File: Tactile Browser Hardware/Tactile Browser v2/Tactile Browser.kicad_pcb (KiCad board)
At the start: 2 copper layers, 100.5 x 125 mm, 79 parts, among them SW1 SW_Push, SW10 SW_Push, SW11 SW_Push, SW12 SW_Push, SW13 SW_Push, SW14 SW_Push, SW15 SW_Push, SW16 SW_Push, SW17 SW_Push, SW18 SW_Push, SW19 SW_Push, SW2 SW_Push, SW20 SW_Push, SW3 SW_Push, SW4 SW_Push, SW5 SW_Push, SW6 SW_Push, SW7 SW_Push, SW8 SW_Push, SW9 SW_Push

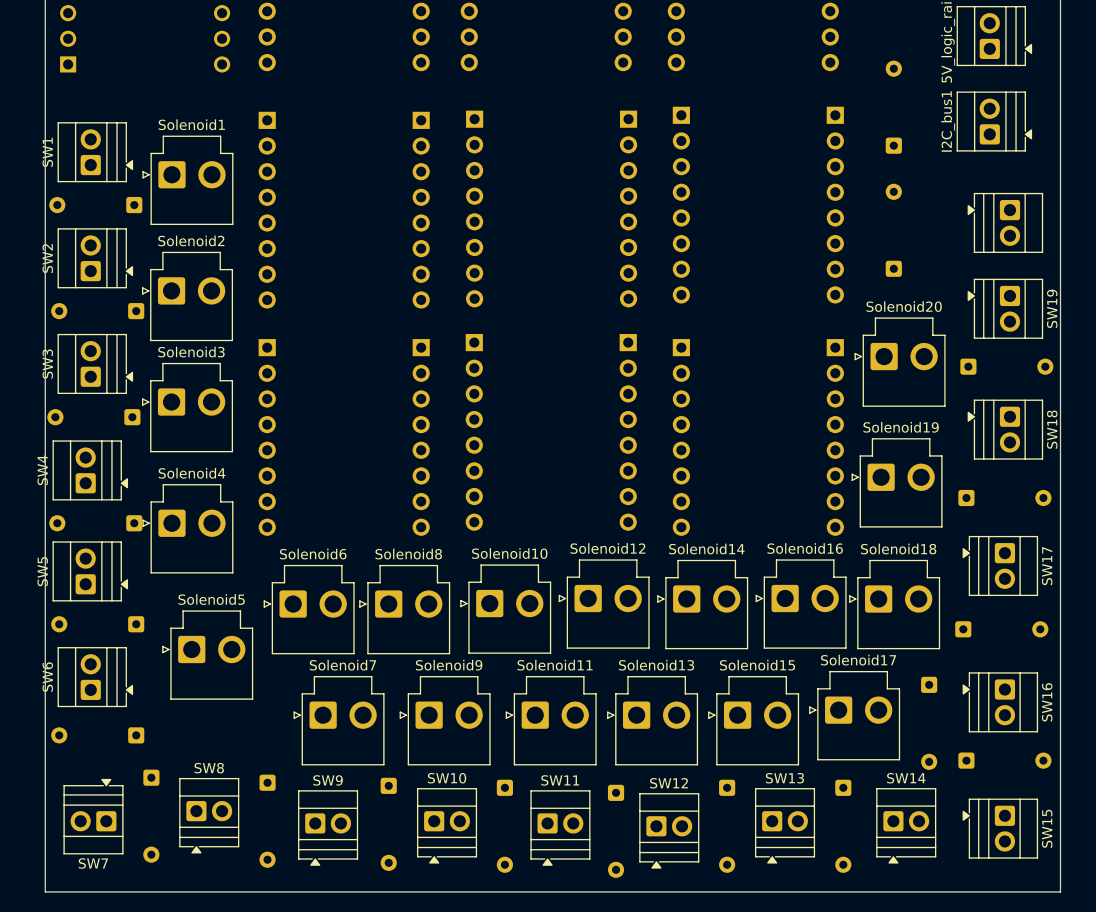
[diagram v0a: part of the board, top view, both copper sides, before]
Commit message: updated solenoid/keyswitch connectors
for ease of manufacturing
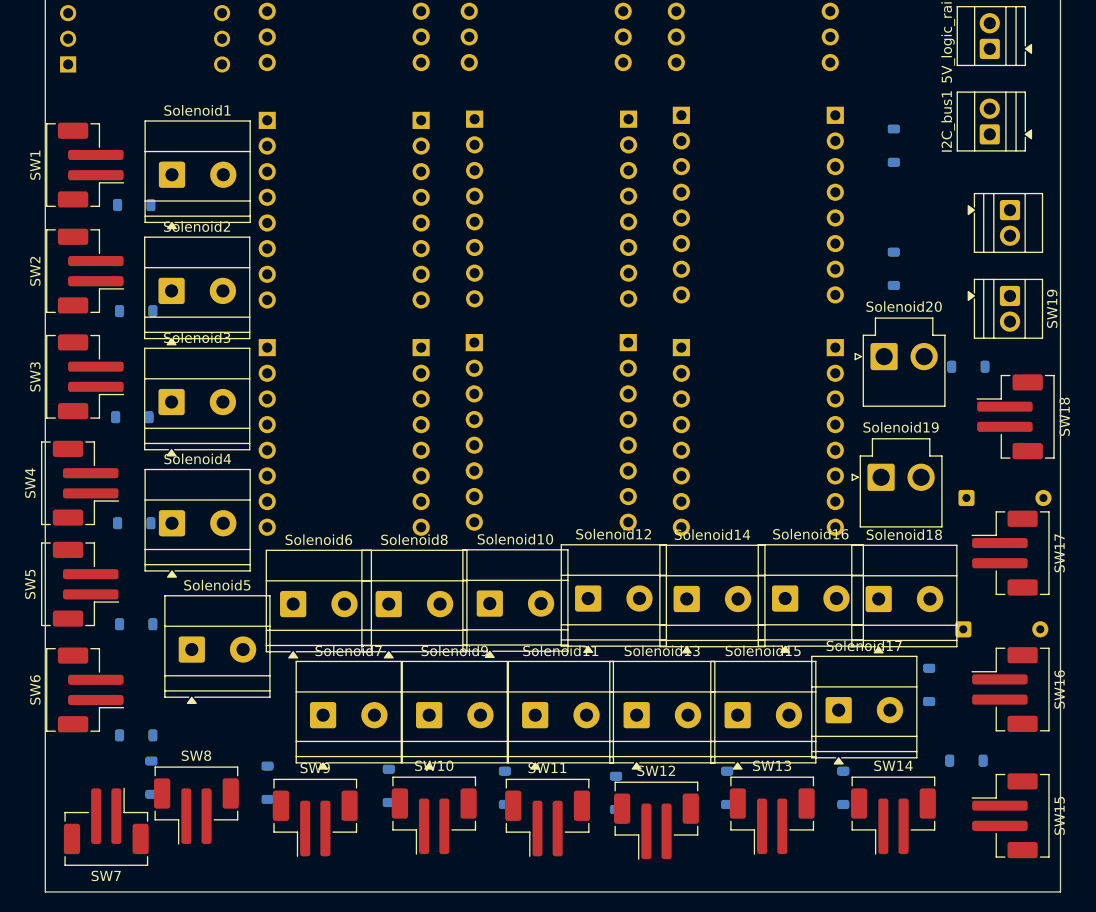
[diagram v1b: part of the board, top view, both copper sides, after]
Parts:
- D1, D10, D11, D12, D13, D14, D15, D18, D19, D2, D20, D3, D4, D5, D6, D7, D8, D9: footprint Diode_THT:D_DO-35_SOD27_P7.62mm_Horizontal -> Diode_SMD:D_SOD-123
- SW1, SW10, SW11, SW12, SW13, SW14, SW15, SW16, SW17, SW18, SW2, SW3, SW4, SW5, SW6, SW7, SW8, SW9: footprint TerminalBlock:TerminalBlock_Xinya_XY308-2.54-2P_1x02_P2.54mm_Horizontal -> Connector_JST:JST_PH_B2B-PH-SM4-TB_1x02-1MP_P2.00mm_Vertical
- Solenoid1: footprint Connector_JST:JST_VH_B2P-VH_1x02_P3.96mm_Vertical -> TerminalBlock_Phoenix:TerminalBlock_Phoenix_MKDS-1,5-2-5.08_1x02_P5.08mm_Horizontal
- Solenoid10, Solenoid11, Solenoid12, Solenoid13, Solenoid14, Solenoid15, Solenoid16, Solenoid17, Solenoid18, Solenoid2, Solenoid3, Solenoid4, Solenoid5, Solenoid6, Solenoid7, Solenoid8, Solenoid9: footprint Connector_JST:JST_VH_B2P-VH-B_1x02_P3.96mm_Vertical -> TerminalBlock_Phoenix:TerminalBlock_Phoenix_MKDS-1,5-2-5.08_1x02_P5.08mm_Horizontal
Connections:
- A1 pad 1: Row2 -> Col2
- A1 pad 10: Col4 -> Row5
- A1 pad 11: Col5 -> Row6
- A1 pad 2: Row1 -> Col1
- A1 pad 5: Row3 -> Col3
- A1 pad 6: Row4 -> Row1
- A1 pad 7: Col1 -> Row2
- A1 pad 8: Col2 -> Row3
- A1 pad 9: Col3 -> Row4
- D1 pad 1: Row1 -> Col1
- D10 pad 1: Row3 -> Col3
- D11 pad 1: Row3 -> Col3
- D12 pad 1: Row3 -> Col3
- D13 pad 1: Row3 -> Col3
- D14 pad 1: Row4 -> Col2
- D15 pad 1: Row4 -> Col3
- D18 pad 1: Row3 -> Col3
- D19 pad 1: Row4 -> Col1
- D2 pad 1: Row1 -> Col1
- D20 pad 1: Row2 -> Col2
- D3 pad 1: Row1 -> Col1
- D4 pad 1: Row1 -> Col1
- D5 pad 1: Row1 -> Col1
- D6 pad 1: Row2 -> Col2
- D7 pad 1: Row2 -> Col2
- D8 pad 1: Row2 -> Col2
- D9 pad 1: Row2 -> Col2
- IO_2 pad 10: unconnected-(IO_2-~{SRCLR}-Pad10) -> 5V
- IO_3 pad 10: unconnected-(IO_3-~{SRCLR}-Pad10) -> 5V
- IO_4 pad 10: unconnected-(IO_4-~{SRCLR}-Pad10) -> 5V
- IO_5 pad 10: unconnected-(IO_5-~{SRCLR}-Pad10) -> 5V
- IO_5 pad 4: S19_in1 -> unconnected-(IO_5-QE-Pad4)
- IO_5 pad 5: S19_in2 -> unconnected-(IO_5-QF-Pad5)
- IO_5 pad 6: S20_in1 -> unconnected-(IO_5-QG-Pad6)
- IO_5 pad 7: S20_in2 -> unconnected-(IO_5-QH-Pad7)
- SW1 pad 2: Col1 -> Row1
- SW10 pad 1: Net-(D20-A) -> Net-(D9-A)
- SW10 pad 2: Col5 -> Row4
- SW11 pad 1: Net-(D18-A) -> Net-(D20-A)
- SW11 pad 2: Col1 -> Row5
- SW12 pad 1: Net-(D10-A) -> Net-(D14-A)
- SW12 pad 2: Col2 -> Row6
- SW13 pad 1: Net-(D11-A) -> Net-(D18-A)
- SW13 pad 2: Col3 -> Row1
- SW14 pad 1: Net-(D12-A) -> Net-(D10-A)
- SW14 pad 2: Col4 -> Row2
- SW15 pad 1: Net-(D13-A) -> Net-(D11-A)
- SW15 pad 2: Col5 -> Row3
- SW16 pad 1: Net-(D19-A) -> Net-(D12-A)
- SW16 pad 2: Col1 -> Row4
- SW17 pad 1: Net-(D14-A) -> Net-(D13-A)
- SW17 pad 2: Col2 -> Row5
- SW18 pad 2: Col3 -> Row6
- SW2 pad 2: Col2 -> Row2
- SW3 pad 2: Col3 -> Row3
- SW4 pad 2: Col4 -> Row4
- SW5 pad 2: Col5 -> Row5
- SW6 pad 1: Net-(D6-A) -> Net-(D19-A)
- SW6 pad 2: Col1 -> Row6
- SW7 pad 1: Net-(D7-A) -> Net-(D6-A)
- SW7 pad 2: Col2 -> Row1
- SW8 pad 1: Net-(D8-A) -> Net-(D7-A)
- SW8 pad 2: Col3 -> Row2
- SW9 pad 1: Net-(D9-A) -> Net-(D8-A)
- SW9 pad 2: Col4 -> Row3

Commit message: pcb design
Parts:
- removed Solenoid19, Solenoid20: Conn_01x02_Pin, Connector_JST:JST_VH_B2P-VH-B_1x02_P3.96mm_Vertical
- A1, D1, D10, D11, D12, D13, D14, D15, D18, D19, D2, D20, D3, D4, D5, D6, D7, D8, D9, Driver1, Driver10, Driver2, Driver3, Driver4, Driver5, Driver6, Driver7, Driver8, Driver9, IO_1, IO_2, IO_3, IO_4, IO_5: moved to F.Cu
- D16, D17: footprint Diode_THT:D_DO-35_SOD27_P7.62mm_Horizontal -> Diode_SMD:D_SOD-123; moved to F.Cu
- moved IO_2 170.0 mm to (209.4, 139.4), turned to 0 degrees
- moved Driver6 151.6 mm to (266.3, 58.9), turned to 0 degrees
- moved Driver7 139.3 mm to (203.8, 47.6), turned to 0 degrees
- moved Driver10 128.4 mm to (150.8, 158.9), turned to 0 degrees
- moved Driver8 109.8 mm to (204.8, 106.6), turned to 0 degrees
- moved Solenoid5 109.3 mm to (130.2, 53.5), turned to 90 degrees
- moved Solenoid3 105.8 mm to (132.5, 39.3), turned to 180 degrees
- moved D5 99.6 mm to (126.3, 68.0), turned to 0 degrees
- moved Driver4 97.5 mm to (168.3, 105.1), turned to 0 degrees
- moved SW6 97.5 mm to (130.2, 92.5), turned to -90 degrees
- moved SW5 97.3 mm to (117.8, 63.1), turned to -90 degrees
- moved D6 94.1 mm to (126.5, 89.0), turned to 0 degrees
- moved D3 91.0 mm to (115.0, 47.5)
- moved Driver5 83.1 mm to (174.3, 51.9), turned to 0 degrees
- moved Solenoid6 79.1 mm to (129.7, 84.5), turned to 90 degrees
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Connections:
- D10 pad 1: Col3 -> Col2
- D11 pad 1: Col3 -> Col2
- D12 pad 1: Col3 -> Col2
- D14 pad 1: Col2 -> Col3
- D16 pad 1: Row4 -> Col3
- D17 pad 1: Row4 -> Col3
- D6 pad 1: Col2 -> Col1
- SW10 pad 1: Net-(D9-A) -> Net-(D10-A)
- SW11 pad 1: Net-(D20-A) -> Net-(D11-A)
- SW12 pad 1: Net-(D14-A) -> Net-(D12-A)
- SW13 pad 1: Net-(D18-A) -> Net-(D13-A)
- SW14 pad 1: Net-(D10-A) -> Net-(D14-A)
- SW15 pad 1: Net-(D11-A) -> Net-(D15-A)
- SW16 pad 1: Net-(D12-A) -> Net-(D16-A)
- SW17 pad 1: Net-(D13-A) -> Net-(D17-A)
- SW18 pad 1: Net-(D15-A) -> Net-(D18-A)
- SW6 pad 1: Net-(D19-A) -> Net-(D6-A)
- SW7 pad 1: Net-(D6-A) -> Net-(D7-A)
- SW8 pad 1: Net-(D7-A) -> Net-(D8-A)
- SW9 pad 1: Net-(D8-A) -> Net-(D9-A)
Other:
- board size 100.5 x 125 mm -> 98.5 x 115.5 mm

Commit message: actually fit everything onto the board I'm a genuis
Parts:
- removed D19, D20: 1N4148, Diode_SMD:D_SOD-123
- removed SW19, SW20: SW_Push, TerminalBlock:TerminalBlock_Xinya_XY308-2.54-2P_1x02_P2.54mm_Horizontal
- moved IO_2 173.5 mm to (49.7, 71.6)
- moved I2C_bus1 154.9 mm to (39.5, 142.5), turned to 0 degrees
- moved Driver7 127.7 mm to (105.8, 129.5)
- moved Driver9 122.9 mm to (61.3, 79.6)
- moved Driver8 119.5 mm to (86.5, 123.5)
- moved Driver4 117.5 mm to (60.8, 57.6)
- moved Driver6 109.8 mm to (158.0, 77.0)
- moved SW18 106.3 mm to (53.5, 140.0), turned to 180 degrees
- moved D18 105.1 mm to (57.0, 136.0), turned to -90 degrees
- moved SW16 99.8 mm to (53.5, 132.0), turned to 0 degrees
- moved D16 99.2 mm to (49.4, 135.8), turned to 90 degrees
- moved 5V_logic_rail1 90.9 mm to (83.0, 144.0), turned to 180 degrees
- moved IO_5 83.5 mm to (82.0, 78.4)
- moved Driver5 83.2 mm to (95.8, 79.6)
- moved Driver10 79.1 mm to (96.3, 101.6)
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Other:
- board size 98.5 x 115.5 mm -> 98.5 x 114.5 mm

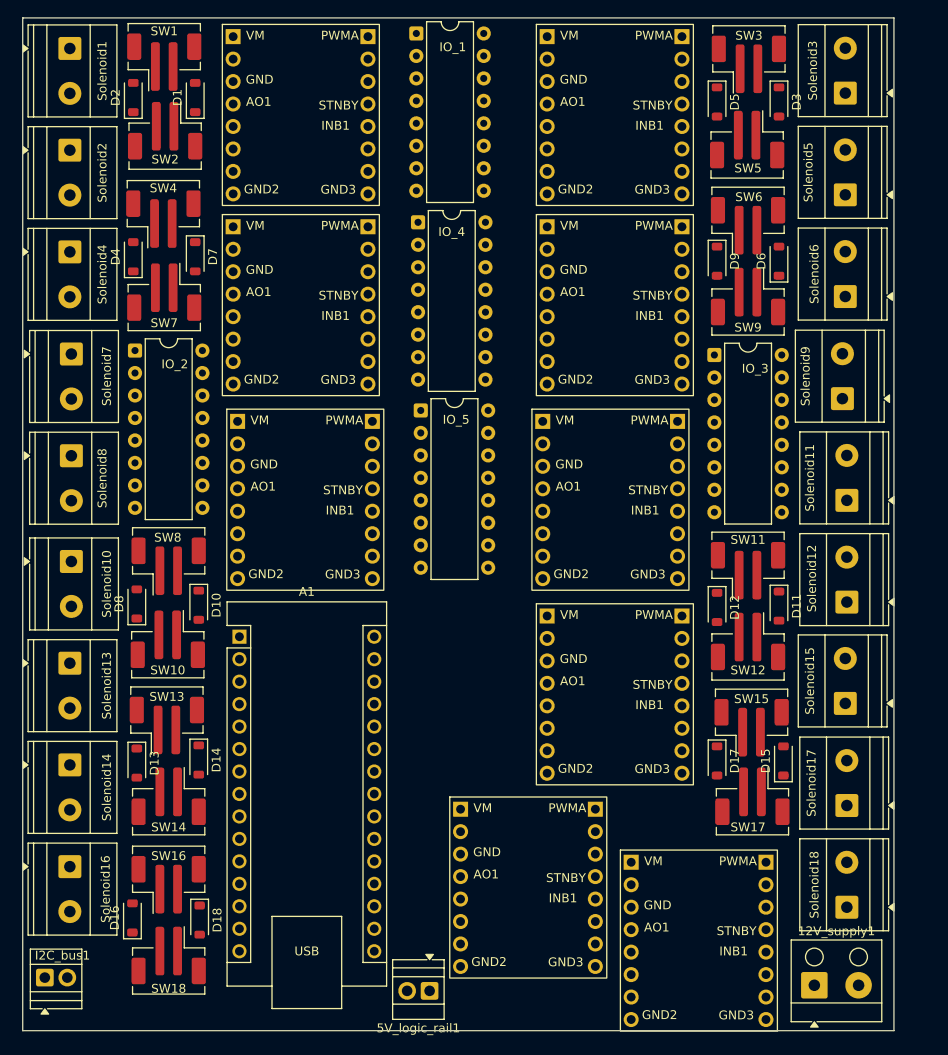
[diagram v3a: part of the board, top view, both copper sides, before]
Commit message: made pcb even smaller
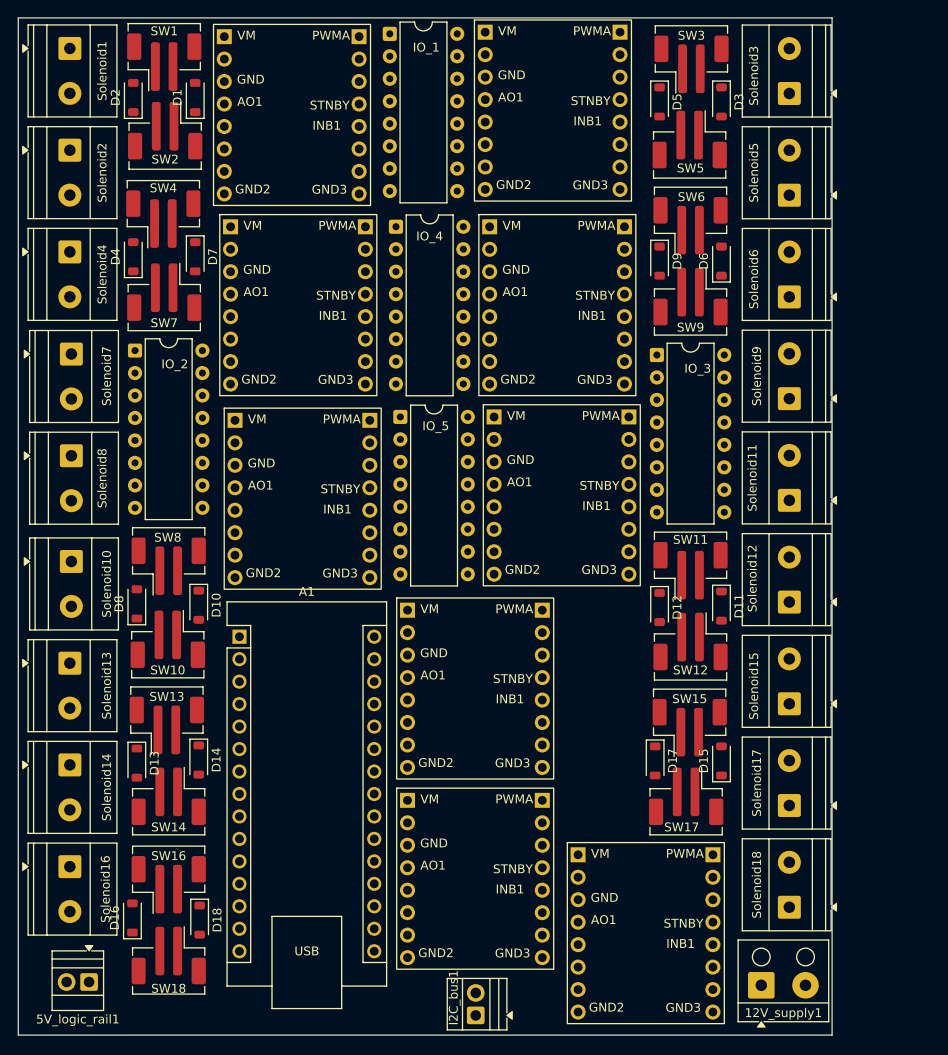
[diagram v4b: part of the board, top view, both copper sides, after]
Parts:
- moved I2C_bus1 48.9 mm to (88.2, 146.8), turned to 90 degrees
- moved 5V_logic_rail1 38.5 mm to (44.5, 143.0)
- moved Driver10 15.8 mm to (80.5, 101.0)
- moved SW17 7.50 mm to (112.0, 122.0)
- moved Driver2 7.02 mm to (89.3, 35.6)
- moved D15 7.00 mm to (116.0, 118.0)
- moved D17 7.00 mm to (108.5, 118.0)
- moved SW15 7.00 mm to (112.4, 114.2)
- moved Solenoid11 6.50 mm to (123.7, 88.5)
- moved Solenoid12 6.50 mm to (123.7, 100.0)
- moved Solenoid17 6.50 mm to (123.7, 123.0)
- moved Solenoid18 6.50 mm to (123.7, 134.5)
- moved D11 6.50 mm to (116.0, 100.5)
- moved D12 6.50 mm to (109.0, 100.7)
- moved D3 6.50 mm to (116.0, 43.5)
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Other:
- board size 98.5 x 114.5 mm -> 92 x 115 mm

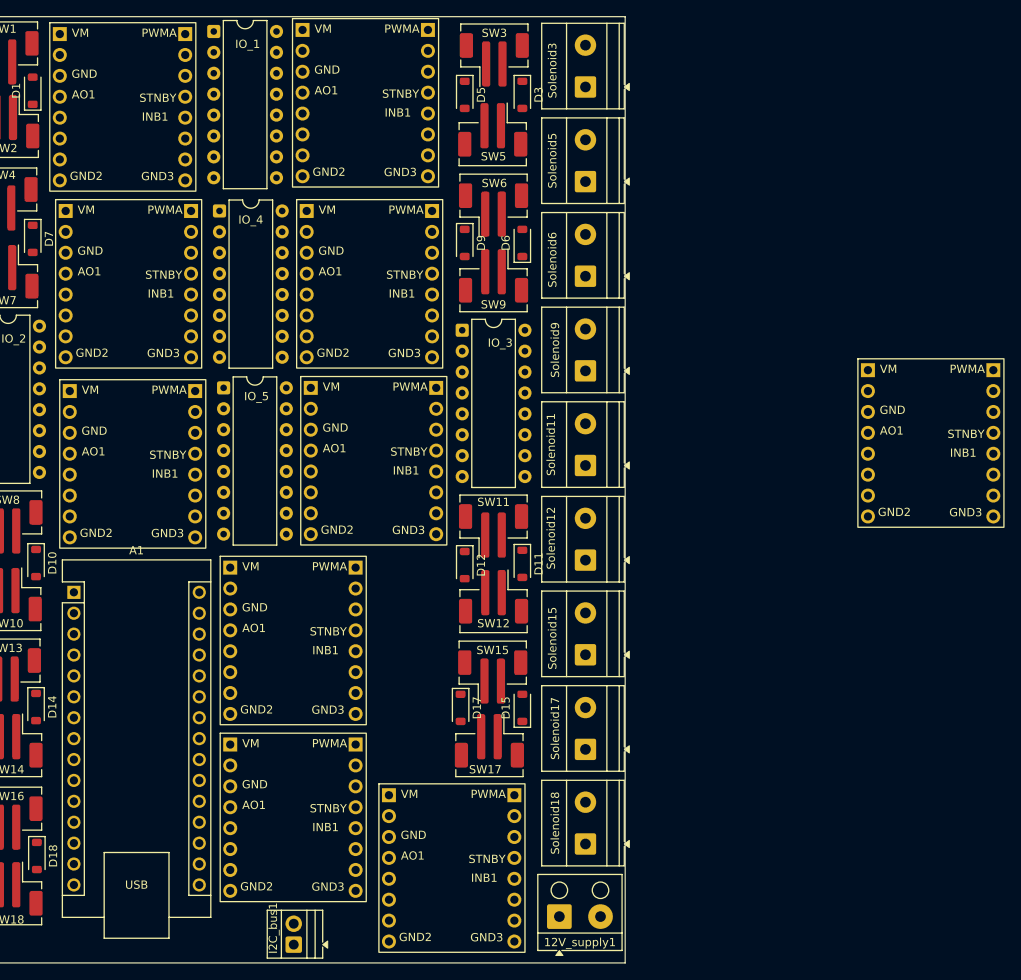
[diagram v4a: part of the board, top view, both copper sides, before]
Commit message: Fixed huge solenoid netting issue
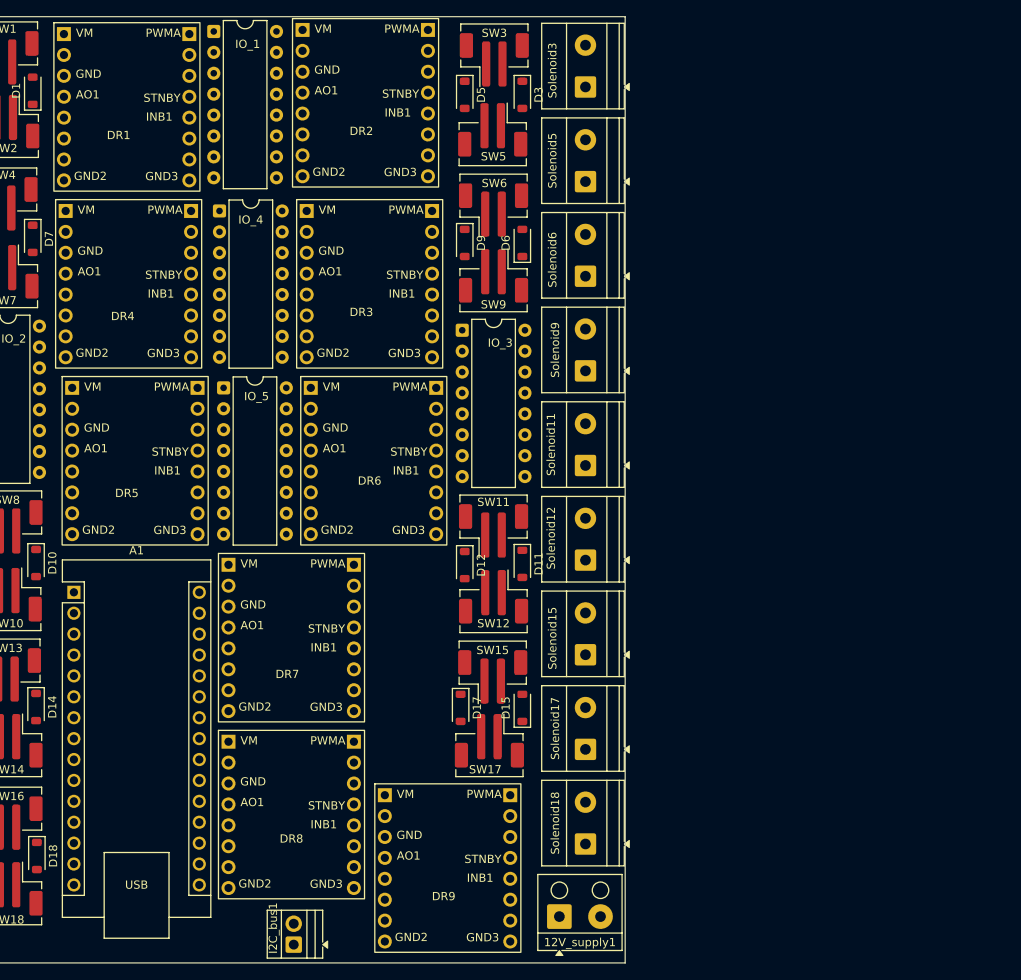
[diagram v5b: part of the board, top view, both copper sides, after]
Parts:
- removed Driver10: TB6612FNG, TB6612FNG_THT:TB6612FNG_DualPinHeader_1x8x2_P2.54mm_Row15.24mm_THT
- moved Driver6 67.7 mm to (90.3, 79.1)
- moved Driver9 62.3 mm to (99.3, 128.6)
- moved Driver7 34.1 mm to (80.3, 100.6)
- moved Driver5 29.0 mm to (61.3, 79.1)
- moved Driver1 0.50 mm to (60.3, 36.1)
- moved Driver8 0.40 mm to (80.3, 122.1)
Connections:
- Solenoid11 pad 1: S19_out1 -> S11_out1
- Solenoid11 pad 2: S19_out2 -> S11_out2
- Solenoid12 pad 1: S20_out1 -> S12_out1
- Solenoid12 pad 2: S20_out2 -> S12_out2
- Solenoid13 pad 1: S18_out1 -> S13_out1
- Solenoid13 pad 2: S18_out2 -> S13_out2
- Solenoid14 pad 1: S17_out1 -> S14_out1
- Solenoid14 pad 2: S17_out2 -> S14_out2
- Solenoid17 pad 1: S14_out1 -> S17_out1
- Solenoid17 pad 2: S14_out2 -> S17_out2
- Solenoid18 pad 1: S13_out1 -> S18_out1
- Solenoid18 pad 2: S13_out2 -> S18_out2
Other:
- board text added: "DR1"
- board text added: "DR2"
- board text added: "DR3"
- board text added: "DR4"
- board text added: "DR5"
- board text added: "DR6"
- board text added: "DR7"
- board text added: "DR8"
- board text added: "DR9"
